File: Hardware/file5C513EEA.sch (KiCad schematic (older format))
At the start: 76 parts, among them J10 IN_2, J11 IN_3, J12 PWM_CV, J4 OUT2_CON, J5 EXT_CON, J6 CUTOFF_CV, J7 SHAPE_CV, J8 OUT1_CON, J9 IN_1, U2 MCP6002-xSN, U3 MCP6004, U4 OPA1678, U5 MCP6002-xSN

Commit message: Updated schematic
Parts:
- removed U2, U5: MCP6002-xSN, Package_SO:SOIC-8_3.9x4.9mm_P1.27mm, symbol Amplifier_Operational:MCP6002-xSN
- added C30: 3.3 nF, Capacitor_SMD:C_0603_1608Metric, symbol Device:C
- added C? (x2): 100 nF, Capacitor_SMD:C_0603_1608Metric, symbol Device:C
- added J7: SET_CV, Connector_Audio:Jack_3.5mm_QingPu_WQP-PJ398SM_Vertical_CircularHoles, symbol Connector:AudioJack2_Ground_Switch
- added R34, R38: 120k, Resistor_SMD:R_0603_1608Metric, symbol Device:R
- added R35: 100k, Resistor_SMD:R_0603_1608Metric, symbol Device:R
- added RV?: SET_ATTEN, Potentiometer_THT:Potentiometer_Bourns_PTA2043_Single_Slide, symbol Device:R_POT_US
- added RV?: PWM_ATTEN, Potentiometer_THT:Potentiometer_Bourns_PTA2043_Single_Slide, symbol Device:R_POT_US
- added unit 5 of U3
- added unit 1 of U3
- added unit 2 of U3
- added unit 3 of U3
- added U5: OPA1678, Package_SO:SOIC-8_3.9x4.9mm_P1.27mm, symbol Amplifier_Operational:MCP6002-xMS
- renumbered C5 to C10, C6 to C11, C65 to C12, C66 to C13, C13 to C14, C14 to C15, C15 to C17, C11 to C18, C12 to C19, C19 to C20, C67 to C21, C68 to C22, C17 to C23, C18 to C24, C20 to C25, C21 to C26, C22 to C27, C23 to C28, C24 to C29, C25 to C31, C26 to C32, C27 to C33, C28 to C34, C7 to C6, C8 to C7, C9 to C8, C10 to C9, D25 to D24, J5 to J13, J6 to J5, J7 to J6, R24 to R25, R25 to R26, R26 to R27, R34 to R36, R35 to R37, R36 to R39, R27 to R40, R37 to R41, R38 to R42, R39 to R43, R40 to R44, R41 to R45, R42 to R46, R43 to R47, R44 to R48, R45 to R49, R46 to R50, R47 to R51, R48 to R52, RV7 to RV6, RV6 to RV7, U4 to U2, U3 to U4
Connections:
- net +12V: now also U5.8 (V+)
- net +3.3VA: now also U3.4 (V+)
- net +3V3: now also RV?.1, RV?.1
- net -10V_REF: now also R34.1
- net -12V: now also U5.4 (V-)
- net CUTOFF_CV: now also U3.7
- net GND: now also C?.2, C?.2, J7.S, J7.TN, RV?.3, RV?.3, U3.10 (+), U3.11 (V-), U3.3 (+), U3.5 (+)
- net SHAPE_CV: now also U3.8
- net at C29.2, R32.2, R33.2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: now also U3.6 (-)
- net at C28.2, R30.2, R31.2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: now also U3.9 (-)
- new net: J7.T, R35.1
- new net: C30.2, R34.2, R35.2, R38.1, U3.2 (-)
- new net PWM_ATTEN: C?.1, RV?.2
- new net SET_ATTEN: C?.1, RV?.2
- new net SET_CV: C30.1, R38.2, U3.1
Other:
- moved on the sheet: C17, D24, J13, R40, RV7, RV9

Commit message: Fixed footprints for new attenuverter pots
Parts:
- RV10, RV11: renamed from RV?; footprint Potentiometer_THT:Potentiometer_Bourns_PTA2043_Single_Slide -> Potentiometer_THT:Potentiometer_Bourns_PTV09A-1_Single_Vertical
- gave numbers to parts that had none: 2
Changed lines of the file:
@@
 P 3350 2100
 AR Path="/5BFD63E3/5BF0EB16" Ref="RV?"  Part="1"
-AR Path="/5BFD63E3/5C513EEB/5BF0EB16" Ref="RV?"  Part="1"
-F 0 "RV?" H 3282 2146 50  0000 R CNN
+AR Path="/5BFD63E3/5C513EEB/5BF0EB16" Ref="RV10"  Part="1"
+F 0 "RV10" H 3282 2146 50  0000 R CNN
 F 1 "SET_ATTEN" H 3282 2055 50  0000 R CNN
-F 2 "Potentiometer_THT:Potentiometer_Bourns_PTA2043_Single_Slide" H 3350 2100 50  0001 C CNN
+F 2 "Potentiometer_THT:Potentiometer_Bourns_PTV09A-1_Single_Vertical" H 3350 2100 50  0001 C CNN
 F 3 "~" H 3350 2100 50  0001 C CNN
 	1    3350 2100
@@
 P 3350 1900
 AR Path="/5BFD63E3/5BF0EB1D" Ref="#PWR?"  Part="1"
-AR Path="/5BFD63E3/5C513EEB/5BF0EB1D" Ref="#PWR?"  Part="1"
-F 0 "#PWR?" H 3350 1750 50  0001 C CNN
+AR Path="/5BFD63E3/5C513EEB/5BF0EB1D" Ref="#PWR0149"  Part="1"
+F 0 "#PWR0149" H 3350 1750 50  0001 C CNN
 F 1 "+3.3V" H 3365 2073 50  0000 C CNN
 F 2 "" H 3350 1900 50  0001 C CNN
@@
 P 3350 2300
 AR Path="/5BFD63E3/5BF0EB24" Ref="#PWR?"  Part="1"
-AR Path="/5BFD63E3/5C513EEB/5BF0EB24" Ref="#PWR?"  Part="1"
-F 0 "#PWR?" H 3350 2050 50  0001 C CNN
+AR Path="/5BFD63E3/5C513EEB/5BF0EB24" Ref="#PWR0150"  Part="1"
+F 0 "#PWR0150" H 3350 2050 50  0001 C CNN
 F 1 "GND" H 3355 2127 50  0000 C CNN
 F 2 "" H 3350 2300 50  0001 C CNN
@@
 P 3550 2300
 AR Path="/5BFD63E3/5BF0EB2D" Ref="C?"  Part="1"
-AR Path="/5BFD63E3/5C513EEB/5BF0EB2D" Ref="C?"  Part="1"
-F 0 "C?" H 3665 2346 50  0000 L CNN
+AR Path="/5BFD63E3/5C513EEB/5BF0EB2D" Ref="C70"  Part="1"
+F 0 "C70" H 3665 2346 50  0000 L CNN
 F 1 "100 nF" H 3665 2255 50  0000 L CNN
 F 2 "Capacitor_SMD:C_0603_1608Metric" H 3588 2150 50  0001 C CNN
@@
 P 3550 2500
 AR Path="/5BFD63E3/5BF0EB37" Ref="#PWR?"  Part="1"
-AR Path="/5BFD63E3/5C513EEB/5BF0EB37" Ref="#PWR?"  Part="1"
-F 0 "#PWR?" H 3550 2250 50  0001 C CNN
+AR Path="/5BFD63E3/5C513EEB/5BF0EB37" Ref="#PWR0153"  Part="1"
+F 0 "#PWR0153" H 3550 2250 50  0001 C CNN
 F 1 "GND" H 3555 2327 50  0000 C CNN
 F 2 "" H 3550 2500 50  0001 C CNN
@@
 P 3350 3150
 AR Path="/5BFD63E3/5BF40470" Ref="RV?"  Part="1"
-AR Path="/5BFD63E3/5C513EEB/5BF40470" Ref="RV?"  Part="1"
-F 0 "RV?" H 3282 3196 50  0000 R CNN
+AR Path="/5BFD63E3/5C513EEB/5BF40470" Ref="RV11"  Part="1"
+F 0 "RV11" H 3282 3196 50  0000 R CNN
 F 1 "PWM_ATTEN" H 3282 3105 50  0000 R CNN
-F 2 "Potentiometer_THT:Potentiometer_Bourns_PTA2043_Single_Slide" H 3350 3150 50  0001 C CNN
+F 2 "Potentiometer_THT:Potentiometer_Bourns_PTV09A-1_Single_Vertical" H 3350 3150 50  0001 C CNN
 F 3 "~" H 3350 3150 50  0001 C CNN
 	1    3350 3150
@@
 P 3350 2950
 AR Path="/5BFD63E3/5BF40477" Ref="#PWR?"  Part="1"
-AR Path="/5BFD63E3/5C513EEB/5BF40477" Ref="#PWR?"  Part="1"
-F 0 "#PWR?" H 3350 2800 50  0001 C CNN
+AR Path="/5BFD63E3/5C513EEB/5BF40477" Ref="#PWR0151"  Part="1"
+F 0 "#PWR0151" H 3350 2800 50  0001 C CNN
 F 1 "+3.3V" H 3365 3123 50  0000 C CNN
 F 2 "" H 3350 2950 50  0001 C CNN
@@
 P 3350 3350
 AR Path="/5BFD63E3/5BF4047E" Ref="#PWR?"  Part="1"
-AR Path="/5BFD63E3/5C513EEB/5BF4047E" Ref="#PWR?"  Part="1"
-F 0 "#PWR?" H 3350 3100 50  0001 C CNN
+AR Path="/5BFD63E3/5C513EEB/5BF4047E" Ref="#PWR0152"  Part="1"
+F 0 "#PWR0152" H 3350 3100 50  0001 C CNN
 F 1 "GND" H 3355 3177 50  0000 C CNN
 F 2 "" H 3350 3350 50  0001 C CNN
@@
 P 3550 3350
 AR Path="/5BFD63E3/5BF40487" Ref="C?"  Part="1"
-AR Path="/5BFD63E3/5C513EEB/5BF40487" Ref="C?"  Part="1"
-F 0 "C?" H 3665 3396 50  0000 L CNN
+AR Path="/5BFD63E3/5C513EEB/5BF40487" Ref="C71"  Part="1"
+F 0 "C71" H 3665 3396 50  0000 L CNN
 F 1 "100 nF" H 3665 3305 50  0000 L CNN
 F 2 "Capacitor_SMD:C_0603_1608Metric" H 3588 3200 50  0001 C CNN
@@
 P 3550 3550
 AR Path="/5BFD63E3/5BF40491" Ref="#PWR?"  Part="1"
-AR Path="/5BFD63E3/5C513EEB/5BF40491" Ref="#PWR?"  Part="1"
-F 0 "#PWR?" H 3550 3300 50  0001 C CNN
+AR Path="/5BFD63E3/5C513EEB/5BF40491" Ref="#PWR0154"  Part="1"
+F 0 "#PWR0154" H 3550 3300 50  0001 C CNN
 F 1 "GND" H 3555 3377 50  0000 C CNN
 F 2 "" H 3550 3550 50  0001 C CNN

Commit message: Board 1 Complete
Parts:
- renumbered U5 to U2
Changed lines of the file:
@@
 $EndComp
 $Comp
-L Amplifier_Operational:MCP6002-xMS U5
+L Amplifier_Operational:MCP6002-xMS U2
 U 3 1 5BEF24B4
 P 5150 7000
-F 0 "U5" H 5108 7046 50  0000 L CNN
+F 0 "U2" H 5108 7046 50  0000 L CNN
 F 1 "OPA1678" H 5108 6955 50  0000 L CNN
 F 2 "Package_SO:SOIC-8_3.9x4.9mm_P1.27mm" H 5150 7000 50  0001 C CNN

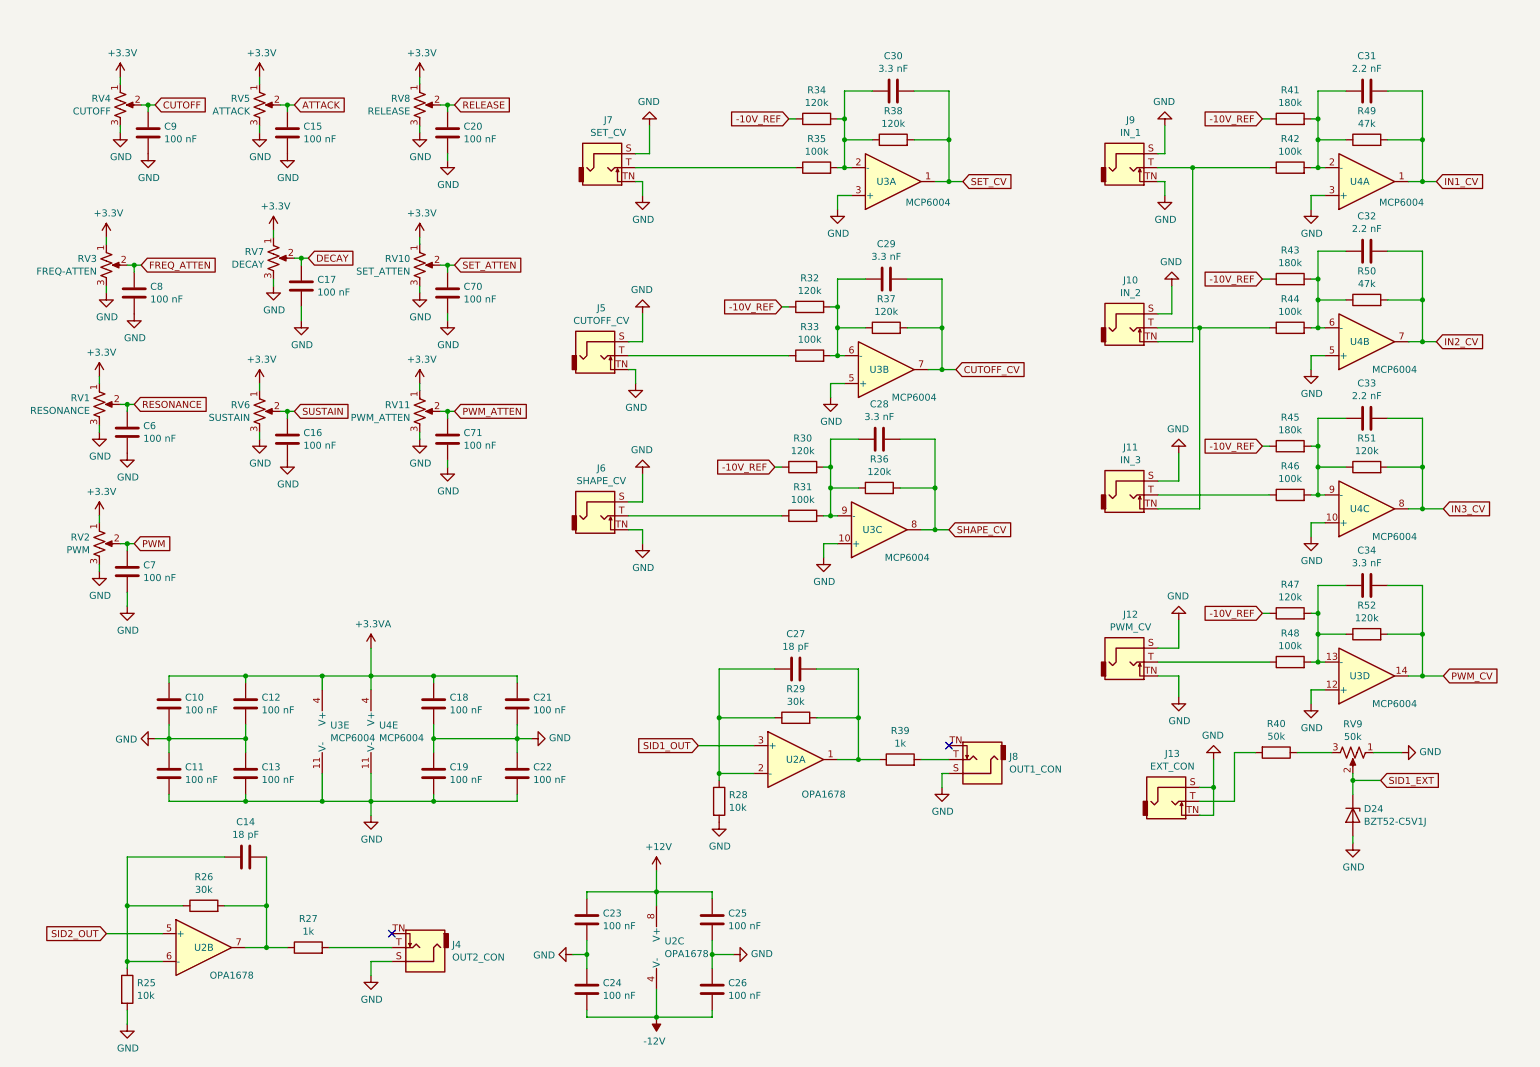
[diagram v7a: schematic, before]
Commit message: Seperated two board with headers
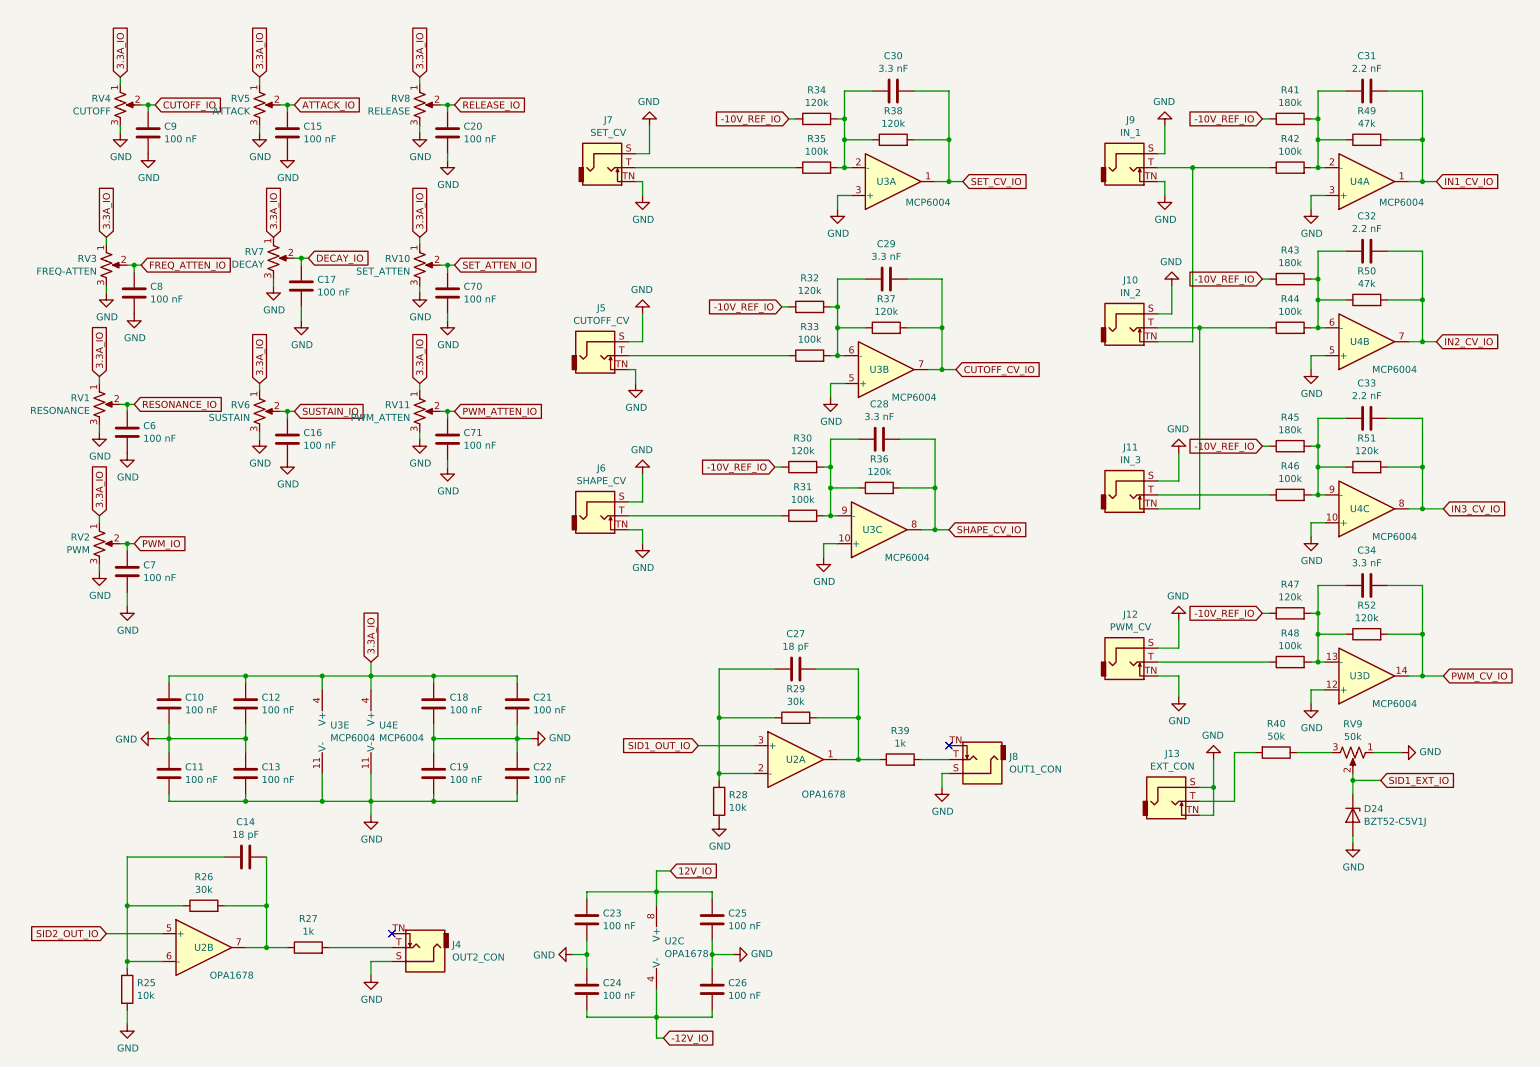
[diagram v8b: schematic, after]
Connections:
- net +3V3 is gone; now on net 3.3A_IO: RV1.1, RV10.1, RV11.1, RV2.1, RV3.1, RV4.1, RV5.1, RV6.1, RV7.1, RV8.1
- net +12V renamed 12V_IO
- net +3.3VA renamed 3.3A_IO
- net -10V_REF renamed -10V_REF_IO
- net -12V renamed -12V_IO
- net ATTACK renamed ATTACK_IO
- net CUTOFF renamed CUTOFF_IO
- net CUTOFF_CV renamed CUTOFF_CV_IO
- net DECAY renamed DECAY_IO
- net FREQ_ATTEN renamed FREQ_ATTEN_IO
- net IN1_CV renamed IN1_CV_IO
- net IN2_CV renamed IN2_CV_IO
- net IN3_CV renamed IN3_CV_IO
- net PWM renamed PWM_IO
- net PWM_ATTEN renamed PWM_ATTEN_IO
- net PWM_CV renamed PWM_CV_IO
- net RELEASE renamed RELEASE_IO
- net RESONANCE renamed RESONANCE_IO
- net SET_ATTEN renamed SET_ATTEN_IO
- net SET_CV renamed SET_CV_IO
- net SHAPE_CV renamed SHAPE_CV_IO
- net SID1_EXT renamed SID1_EXT_IO
- net SID1_OUT renamed SID1_OUT_IO
- net SID2_OUT renamed SID2_OUT_IO
- net SUSTAIN renamed SUSTAIN_IO
